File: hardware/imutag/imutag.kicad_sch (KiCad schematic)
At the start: 26 parts, among them J201 CONN_02X04, J301 Conn_01x01, J302 Conn_01x01, J303 Conn_01x01, J304 Conn_01x01, J401 CONN_01X02, Q501 Q_NPN_BEC, U2 AK09940A, U3 LPS22DF, U302 stm32l431kc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

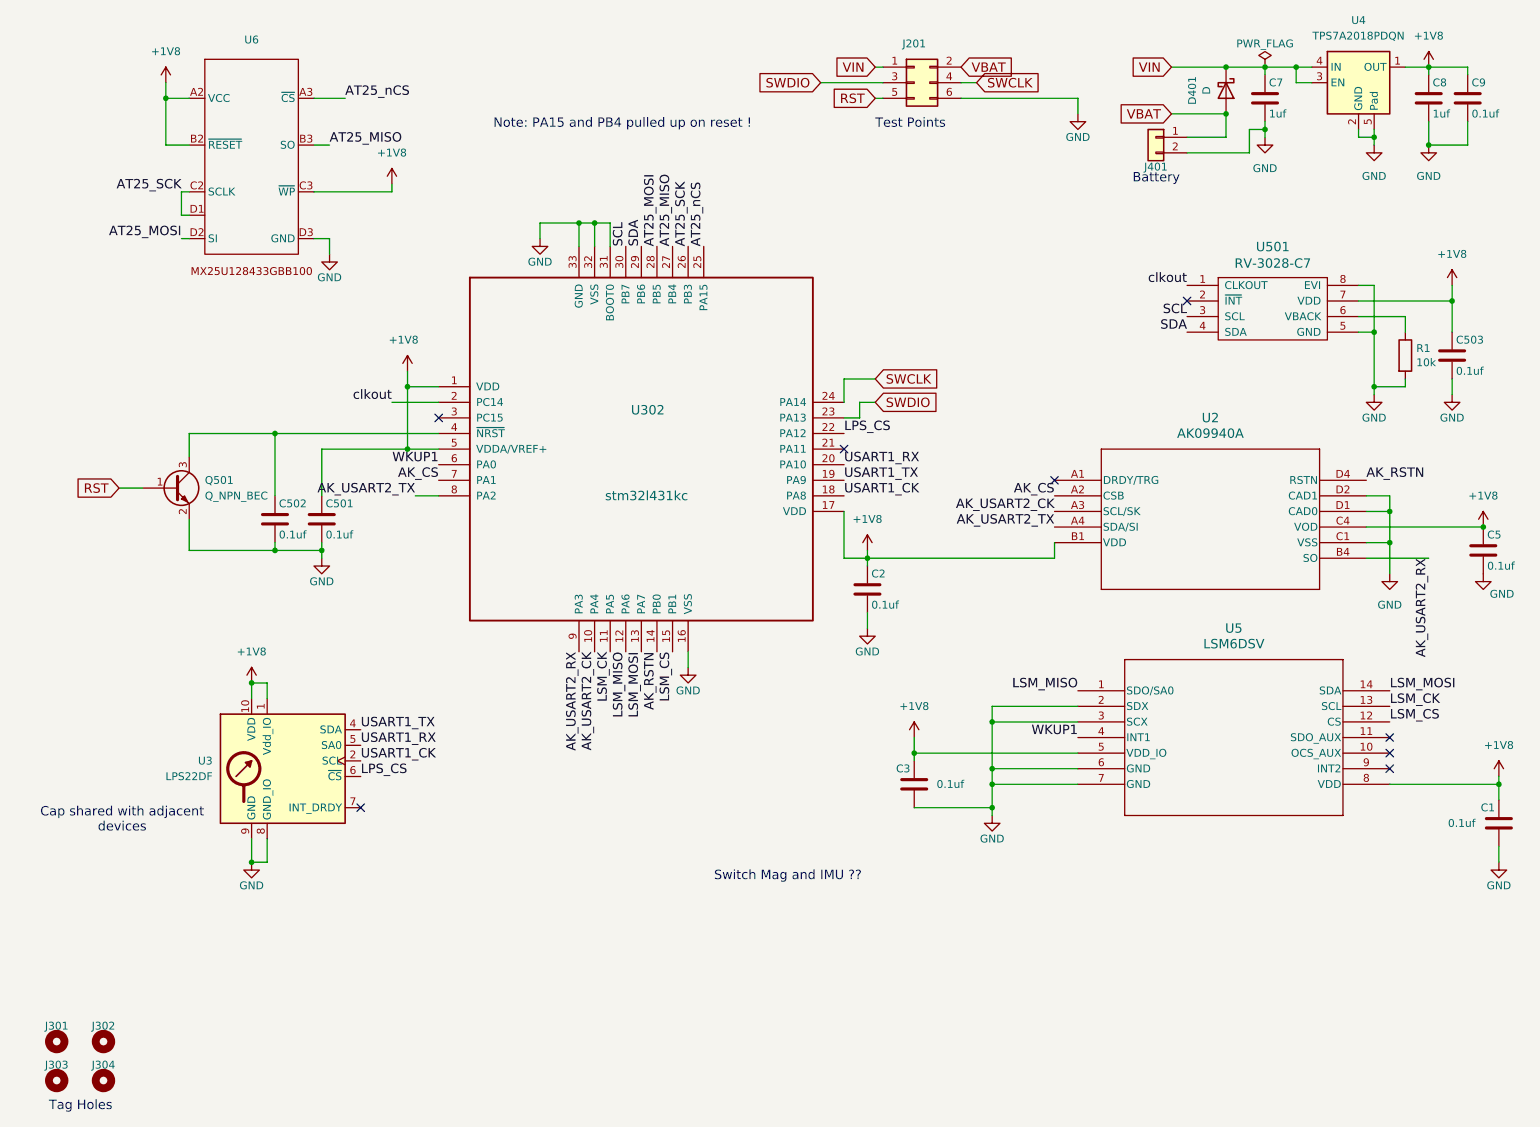
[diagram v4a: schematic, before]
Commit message: imu tag breakout
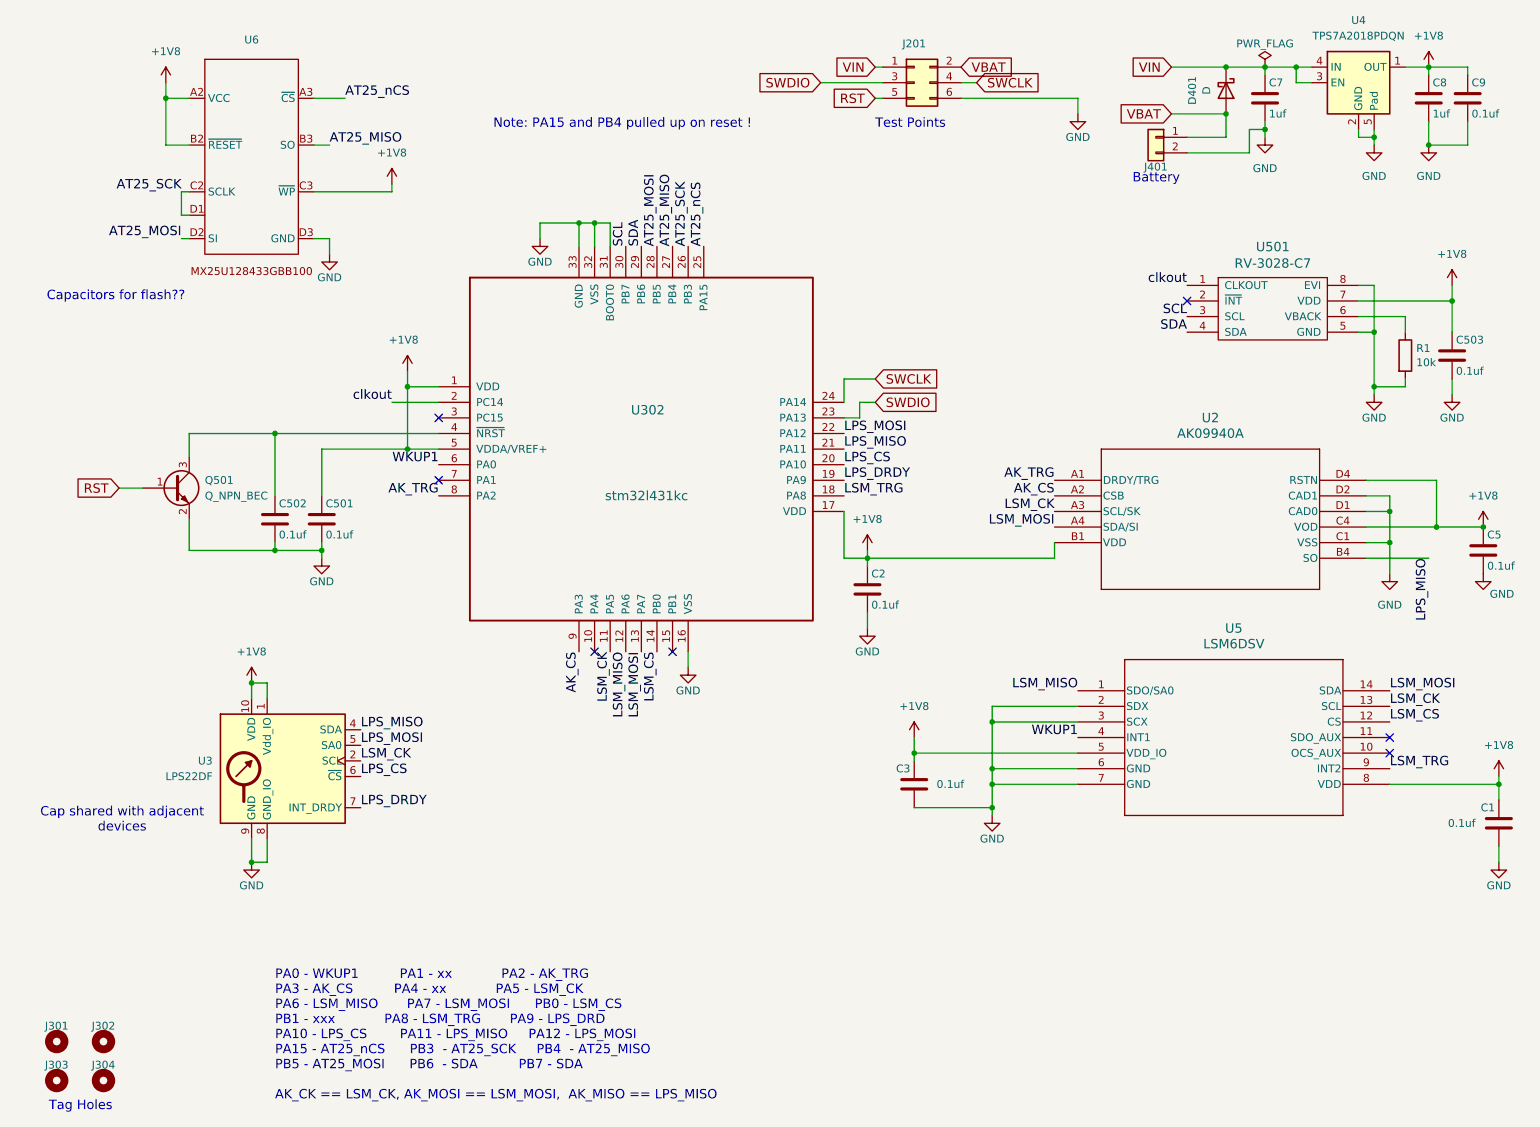
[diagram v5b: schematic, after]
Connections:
- net +1V8: now also U2.D4 (RSTN)
- net AK_CS: now also U302.9 (PA3); no longer U302.7 (PA1)
- net LPS_CS: now also U302.20 (PA10); no longer U302.22 (PA12)
- net LSM_CK: now also U2.A3 (SCL/SK), U3.2 (SCL)
- net LSM_CS: now also U302.14 (PB0); no longer U302.15 (PB1)
- net LSM_MOSI: now also U2.A4 (SDA/SI)
- net LPS_MISO: now reaches U302.21 (PA11)
- net LPS_MISO: now also U2.B4 (SO), U3.4 (SDA)
- net LSM_TRG: now reaches U5.9 (INT2)
- net LSM_TRG: now also U302.18 (PA8)
- net AK_TRG: now reaches U2.A1 (DRDY/TRG)
- net AK_TRG: now also U302.8 (PA2)
- net LPS_DRDY: now reaches U3.7 (INT_DRDY)
- net LPS_DRDY: now also U302.19 (PA9)
- removed net AK_RSTN: U2.D4 (RSTN), U302.14 (PB0)
- net AK_USART2_CK: no longer names the net of U302.10 (PA4)
- net AK_USART2_CK: no longer U2.A3 (SCL/SK)
- removed net AK_USART2_RX: U2.B4 (SO), U302.9 (PA3)
- removed net AK_USART2_TX: U2.A4 (SDA/SI), U302.8 (PA2)
- removed net USART1_CK: U3.2 (SCL), U302.18 (PA8)
- net USART1_RX renamed LPS_MOSI
- net LPS_MOSI: now also U302.22 (PA12); no longer U302.20 (PA10)
- removed net USART1_TX: U3.4 (SDA), U302.19 (PA9)
- no-connect marks 8 -> 7
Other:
- note added: "Capacitors for flash??"
- note added: "PA0 - WKUP1 PA1 - xx PA2 - AK_TRG PA3 - AK_CS PA4 - xx PA5 - LSM_CK PA6 - LSM_MISO PA7 - LSM_MOSI PB0 - LSM_CS PB1 - xxx PA8 - LSM_TRG PA9 - LPS_DRD PA10 - LPS_CS PA11 - LPS_MISO PA12 - LPS_MOSI PA15 - AT25_nCS PB3 - AT25_SCK PB4 - AT25_MISO PB5 - AT25_MOSI PB6 - SDA PB7 - SDA AK_CK == LSM_CK, AK_MOSI == LSM_MOSI, AK_MISO == LPS_MISO"
- note removed: "Switch Mag and IMU ??"
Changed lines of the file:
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@@
 (kicad_sch
-	(version 20231120)
+	(version 20250114)
 	(generator "eeschema")
-	(generator_version "8.0")
+	(generator_version "9.0")
 	(paper "USLetter")
 	(title_block
@@
 		(comment 1 "Geoffrey Brown")
 	)
+	(text "Note: PA15 and PB4 pulled up on reset !"
+		(exclude_from_sim no)
+		(at 96.52 34.29 0)
+		(effects
+			(font
+				(size 1.524 1.524)
+			)
+			(justify left bottom)
+		)
+	)
+	(text "Capacitors for flash??"
+		(exclude_from_sim no)
+		(at 35.052 61.468 0)
+		(effects
+			(font
+				(size 1.524 1.524)
+			)
+		)
+	)
+	(text "Tag Holes"
+		(exclude_from_sim no)
+		(at 24.13 194.31 0)
+		(effects
+			(font
+				(size 1.524 1.524)
+			)
+			(justify left bottom)
+		)
+	)
+	(text "Test Points"
+		(exclude_from_sim no)
+		(at 158.75 34.29 0)
+		(effects
+			(font
+				(size 1.524 1.524)
+			)
+			(justify left bottom)
+		)
+	)
+	(text "PA0 - WKUP1          PA1 - xx            PA2 - AK_TRG\nPA3 - AK_CS          PA4 - xx            PA5 - LSM_CK\nPA6 - LSM_MISO       PA7 - LSM_MOSI      PB0 - LSM_CS\nPB1 - xxx            PA8 - LSM_TRG       PA9 - LPS_DRD\nPA10 - LPS_CS        PA11 - LPS_MISO     PA12 - LPS_MOSI\nPA15 - AT25_nCS      PB3  - AT25_SCK     PB4  - AT25_MISO\nPB5 - AT25_MOSI      PB6  - SDA          PB7 - SDA\n\nAK_CK == LSM_CK, AK_MOSI == LSM_MOSI,  AK_MISO == LPS_MISO"
+		(exclude_from_sim no)
+		(at 60.96 181.864 0)
+		(effects
+			(font
+				(face "Courier")
+				(size 1.524 1.524)
+			)
+			(justify left)
+		)
+	)
+	(text "Battery"
+		(exclude_from_sim no)
+		(at 200.66 43.18 0)
+		(effects
+			(font
+				(size 1.524 1.524)
+			)
+			(justify left bottom)
+		)
+	)
+	(text "Cap shared with adjacent\ndevices"
+		(exclude_from_sim no)
+		(at 36.068 146.812 0)
+		(effects
+			(font
+				(size 1.524 1.524)
+			)
+		)
+	)
 	(junction
 		(at 248.92 24.13)
@@
 	)
 	(junction
+		(at 250.19 99.06)
+		(diameter 0)
+		(color 0 0 0 0)
+	)
+	(junction
 		(at 113.03 49.53)
 		(diameter 0)
@@
 	)
 	(no_connect
-		(at 187.96 91.44)
-	)
-	(no_connect
-		(at 153.67 86.36)
+		(at 113.03 119.38)
 	)
 	(no_connect
-		(at 74.93 144.78)
+		(at 87.63 91.44)
 	)
 	(no_connect
-		(at 242.57 138.43)
+		(at 125.73 119.38)
 	)
 	(no_connect
@@
 	(wire
 		(pts
+			(xy 250.19 99.06) (xy 257.81 99.06)
+		)
+		(stroke
+			(width 0)
+			(type default)
+		)
+	)
+	(wire
+		(pts
 			(xy 207.01 24.13) (xy 215.9 24.13)
 		)
@@
 	(wire
 		(pts
+			(xy 250.19 91.44) (xy 250.19 99.06)
+		)
+		(stroke
+			(width 0)
+			(type default)
+		)
+	)
+	(wire
+		(pts
 			(xy 82.55 73.66) (xy 82.55 76.2)
 		)
@@
 	(wire
 		(pts
+			(xy 238.76 91.44) (xy 250.19 91.44)
+		)
+		(stroke
+			(width 0)
+			(type default)
+		)
+	)
+	(wire
+		(pts
 			(xy 237.49 64.77) (xy 245.11 64.77)
 		)
@@
 	(wire
 		(pts
-			(xy 238.76 99.06) (xy 257.81 99.06)
+			(xy 238.76 99.06) (xy 250.19 99.06)
 		)
 		(stroke
@@
 	(wire
 		(pts
-			(xy 83.82 93.98) (xy 87.63 93.98)
-		)
-		(stroke
-			(width 0)
-			(type default)
-		)
-	)
-	(wire
-		(pts
 			(xy 69.85 52.07) (xy 69.85 54.61)
 		)
@@
 		)
 	)
-	(text "Note: PA15 and PB4 pulled up on reset !"
-		(exclude_from_sim no)
-		(at 96.52 34.29 0)
-		(effects
-			(font
-				(size 1.524 1.524)
-			)
-			(justify left bottom)
-		)
-	)
-	(text "Tag Holes"
-		(exclude_from_sim no)
-		(at 24.13 194.31 0)
-		(effects
-			(font
-				(size 1.524 1.524)
-			)
-			(justify left bottom)
-		)
-	)
-	(text "Test Points"
-		(exclude_from_sim no)
-		(at 158.75 34.29 0)
-		(effects
-			(font
-				(size 1.524 1.524)
-			)
-			(justify left bottom)
-		)
-	)
-	(text "Battery"
-		(exclude_from_sim no)
-		(at 200.66 43.18 0)
-		(effects
-			(font
-				(size 1.524 1.524)
-			)
-			(justify left bottom)
-		)
-	)
-	(text "Switch Mag and IMU ??"
-		(exclude_from_sim no)
-		(at 144.526 155.956 0)
-		(effects
-			(font
-				(size 1.524 1.524)
-			)
-		)
-	)
-	(text "Cap shared with adjacent\ndevices"
-		(exclude_from_sim no)
-		(at 36.068 146.812 0)
-		(effects
-			(font
-				(size 1.524 1.524)
-			)
-		)
-	)
-	(label "USART1_CK"
-		(at 153.67 93.98 0)
-		(effects
-			(font
-				(size 1.524 1.524)
-			)
-			(justify left bottom)
-		)
-	)
-	(label "USART1_TX"
-		(at 153.67 91.44 0)
-		(effects
-			(font
-				(size 1.524 1.524)
-			)
-			(justify left bottom)
-		)
-	)
 	(label "LSM_CK"
 		(at 115.57 119.38 270)
@@
 		)
 	)
-	(label "AK_RSTN"
-		(at 123.19 119.38 270)
-		(effects
-			(font
-				(size 1.524 1.524)
-			)
-			(justify right bottom)
-		)
-	)
-	(label "USART1_CK"
+	(label "LSM_CK"
 		(at 74.93 137.16 0)
 		(effects
@@
 		)
 	)
-	(label "USART1_RX"
-		(at 153.67 88.9 0)
+	(label "LPS_DRDY"
+		(at 153.67 91.44 0)
 		(effects
 			(font
@@
 		)
 	)
-	(label "AK_USART2_RX"
-		(at 110.49 119.38 270)
+	(label "LSM_MISO"
+		(at 191.77 125.73 180)
 		(effects
 			(font
@@
 		)
 	)
-	(label "LSM_MISO"
-		(at 191.77 125.73 180)
+	(label "AK_CS"
+		(at 187.96 93.98 180)
 		(effects
 			(font
@@
 		)
 	)
-	(label "AK_CS"
-		(at 187.96 93.98 180)
+	(label "clkout"
+		(at 80.01 78.74 180)
 		(effects
 			(font
@@
 		)
 	)
-	(label "clkout"
-		(at 80.01 78.74 180)
+	(label "AK_TRG"
+		(at 187.96 91.44 180)
+		(effects
+			(font
+				(size 1.524 1.524)
+			)
+			(justify right bottom)
+		)
+	)
+	(label "AK_CS"
+		(at 110.49 119.38 270)
 		(effects
 			(font
@@
 	)
 	(label "LSM_CS"
-		(at 125.73 119.38 270)
+		(at 123.19 119.38 270)
 		(effects
 			(font
@@
 		)
 	)
-	(label "AK_USART2_CK"
-		(at 113.03 119.38 270)
+	(label "LPS_DRDY"
+		(at 74.93 144.78 0)
 		(effects
 			(font
 				(size 1.524 1.524)
 			)
-			(justify right bottom)
+			(justify left bottom)
 		)
 	)
-	(label "AK_CS"
-		(at 87.63 91.44 180)
+	(label "LSM_TRG"
+		(at 153.67 93.98 0)
+		(effects
+			(font
+				(size 1.524 1.524)
+			)
+			(justify left bottom)
+		)
+	)
+	(label "AK_TRG"
+		(at 87.63 93.98 180)
 		(effects
 			(font
@@
 		)
 	)
-	(label "AK_USART2_CK"
+	(label "LSM_CK"
 		(at 187.96 96.52 180)
 		(effects
@@
 		)
 	)
-	(label "USART1_TX"
+	(label "LPS_MISO"
 		(at 74.93 132.08 0)
 		(effects
@@
 	)
 	(label "LPS_CS"
-		(at 153.67 83.82 0)
+		(at 153.67 88.9 0)
 		(effects
 			(font
@@
 		)
 	)
-	(label "AT25_SCK"
-		(at 128.27 53.34 90)
+	(label "LPS_MISO"
+		(at 153.67 86.36 0)
 		(effects
 			(font
@@
 		)
 	)
-	(label "AT25_MISO"
-		(at 69.85 36.83 0)
+	(label "LPS_MOSI"
+		(at 153.67 83.82 0)
 		(effects
 			(font
@@
 		)
 	)
-	(label "AK_RSTN"
-		(at 238.76 91.44 0)
+	(label "LSM_TRG"
+		(at 242.57 138.43 0)
 		(effects
 			(font
@@
 		)
 	)
-	(label "AK_USART2_TX"
-		(at 187.96 99.06 180)
+	(label "AT25_SCK"
+		(at 128.27 53.34 90)
 		(effects
 			(font
 				(size 1.524 1.524)
 			)
-			(justify right bottom)
+			(justify left bottom)
 		)
 	)
-	(label "SCL"
-		(at 209.55 64.77 180)
+	(label "AT25_MISO"
+		(at 69.85 36.83 0)
+		(effects
+			(font
+				(size 1.524 1.524)
+			)
+			(justify left bottom)
+		)
+	)
+	(label "LSM_MOSI"
+		(at 187.96 99.06 180)
 		(effects
 			(font
@@
 		)
 	)
-	(label "LSM_MISO"
-		(at 118.11 119.38 270)
+	(label "SCL"
+		(at 209.55 64.77 180)
 		(effects
 			(font
@@
 		)
 	)
-	(label "AK_USART2_TX"
-		(at 83.82 93.98 180)
+	(label "LSM_MISO"
+		(at 118.11 119.38 270)
 		(effects
 			(font
@@
 		)
 	)
-	(label "AK_USART2_RX"
+	(label "LPS_MISO"
 		(at 248.92 104.14 270)
 		(effects
@@
 		)
 	)
-	(label "USART1_RX"
+	(label "LPS_MOSI"
 		(at 74.93 134.62 0)
 		(effects
@@
 		)
 	)
+	(embedded_fonts no)
 )

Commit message: checkpoint
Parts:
- added C4: 4.7uf, Capacitor_SMD:C_0201_0603Metric, symbol Device:C
- C1, C3, C501, C502, C503: MPN C181047 -> GRM033C81E104KE14D
- C2: LCSC C76929 -> C181047; MFN murata -> Murata; MPN GRM033R60J105MEA2D -> GRM033C81E104KE14D
- C5, C9: LCSC (none) -> C181047
- C7, C8: LCSC (none) -> C76930
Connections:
- net GND: now also C4.1; no longer U302.31 (BOOT0)
- new net: C4.2, U302.31 (BOOT0)
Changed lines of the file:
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@@
 	)
 	(junction
+		(at 104.14 49.53)
+		(diameter 0)
+		(color 0 0 0 0)
+	)
+	(junction
 		(at 177.8 130.81)
 		(diameter 0)
@@
 	)
 	(junction
-		(at 113.03 49.53)
-		(diameter 0)
-		(color 0 0 0 0)
-	)
-	(junction
 		(at 260.35 140.97)
 		(diameter 0)
@@
 	(wire
 		(pts
+			(xy 104.14 41.91) (xy 115.57 41.91)
+		)
+		(stroke
+			(width 0)
+			(type default)
+		)
+	)
+	(wire
+		(pts
 			(xy 260.35 140.97) (xy 260.35 143.51)
 		)
@@
 	(wire
 		(pts
-			(xy 113.03 49.53) (xy 115.57 49.53)
-		)
-		(stroke
-			(width 0)
-			(type default)
-		)
-	)
-	(wire
-		(pts
 			(xy 238.76 93.98) (xy 242.57 93.98)
 		)
@@
 	(wire
 		(pts
-			(xy 115.57 49.53) (xy 115.57 53.34)
+			(xy 115.57 41.91) (xy 115.57 53.34)
 		)
 		(stroke
@@
 			)
 		)
-		(property "MPN" "C181047"
+		(property "MPN" "GRM033C81E104KE14D"
 			(at 60.96 97.79 0)
 			(effects
@@
 			)
 		)
-		(property "MPN" "C181047"
+		(property "MPN" "GRM033C81E104KE14D"
 			(at 68.58 97.79 0)
 			(effects
@@
 			)
 		)
-		(property "MPN" "C181047"
+		(property "MPN" "GRM033C81E104KE14D"
 			(at 252.73 71.12 0)
 			(effects
@@
 			)
 		)
-		(property "MPN" "C181047"
+		(property "MPN" "GRM033C81E104KE14D"
 			(at 438.15 250.19 0)
 			(effects
@@
 			)
 		)
-		(property "MFN" "murata"
+		(property "MFN" "Murata"
 			(at 157.48 109.22 0)
 			(effects
@@
 			)
 		)
-		(property "MPN" "GRM033R60J105MEA2D"
+		(property "MPN" "GRM033C81E104KE14D"
 			(at 157.48 109.22 0)
 			(effects
@@
 			)
 		)
-		(property "LCSC" "C76929"
+		(property "LCSC" "C181047"
 			(at 157.48 109.22 0)
 			(effects
@@
 			)
 		)
+		(property "LCSC" "C181047"
+			(at 255.27 29.21 0)
+			(effects
+				(font
+					(size 1.27 1.27)
+				)
+				(hide yes)
+			)
+		)
 		(pin "1"
 		)
@@
 			)
 		)
+		(property "LCSC" "C76930"
+			(at 248.92 29.21 0)
+			(effects
+				(font
+					(size 1.27 1.27)
+				)
+				(hide yes)
+			)
+		)
 		(pin "1"
 		)
@@
 			)
 		)
+		(property "LCSC" "C181047"
+			(at 257.81 102.87 0)
+			(effects
+				(font
+					(size 1.27 1.27)
+				)
+				(hide yes)
+			)
+		)
 		(pin "1"
 		)
@@
 			)
 		)
+		(property "LCSC" "C76930"
+			(at 222.25 29.21 0)
+			(effects
+				(font
+					(size 1.27 1.27)
+				)
+				(hide yes)
+			)
+		)
 		(pin "1"
 		)
@@
 	)
 	(symbol
+		(lib_id "Device:C")
+		(at 104.14 45.72 180)
+		(unit 1)
+		(exclude_from_sim no)
+		(in_bom yes)
+		(on_board yes)
+		(dnp no)
+		(fields_autoplaced yes)
+		(property "Reference" "C4"
+			(at 107.95 44.4499 0)
+			(effects
+				(font
+					(size 1.27 1.27)
+				)
+				(justify right)
+			)
+		)
+		(property "Value" "4.7uf"
+			(at 107.95 46.9899 0)
+			(effects
+				(font
+					(size 1.27 1.27)
+				)
+				(justify right)
+			)
+		)
+		(property "Footprint" "Capacitor_SMD:C_0201_0603Metric"
+			(at 103.1748 41.91 0)
+			(effects
+				(font
+					(size 1.27 1.27)
+				)
+				(hide yes)
+			)
+		)
+		(property "Datasheet" "~"
+			(at 104.14 45.72 0)
+			(effects
+				(font
+					(size 1.27 1.27)
+				)
+				(hide yes)
+			)
+		)
+		(property "Description" "Unpolarized capacitor"
+			(at 104.14 45.72 0)
+			(effects
+				(font
+					(size 1.27 1.27)
+				)
+				(hide yes)
+			)
+		)
+		(property "LCSC" "C335103"
+			(at 104.14 45.72 0)
+			(effects
+				(font
+					(size 1.27 1.27)
+				)
+				(hide yes)
+			)
+		)
+		(property "MFN" "Murata"
+			(at 104.14 45.72 0)
+			(effects
+				(font
+					(size 1.27 1.27)
+				)
+				(hide yes)
+			)
+		)
+		(property "MPN" "GRM035R60J475ME15D"
+			(at 104.14 45.72 0)
+			(effects
+				(font
+					(size 1.27 1.27)
+				)
+				(hide yes)
+			)
+		)
+		(pin "1"
+		)
+		(pin "2"
+		)
+		(instances
+			(project ""
+				(path "/e44ca67a-43be-444b-8652-f54825a2eb6f"
+					(reference "C4")
+					(unit 1)
+				)
+			)
+		)
+	)
+	(symbol
 		(lib_id "power:GND")
 		(at 240.03 77.47 0)
@@
 			)
 		)
-		(property "MPN" "C181047"
+		(property "MPN" "GRM033C81E104KE14D"
 			(at 342.9 243.84 0)
 			(effects

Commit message: checkpoint
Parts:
- U4: value TPS7A2018PDQN -> TPS7A0218PDQNR; DISTPN 296-TPS7A2018PDQNRCT-ND -> 296-TPS7A0218PDQNRTR-ND; LCSC (none) -> C2862166; MPN TPS7A2018PDQNR -> TPS7A0218PDQNR
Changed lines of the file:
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@@
 			)
 		)
-		(property "Value" "TPS7A2018PDQN"
+		(property "Value" "TPS7A0218PDQNR"
 			(at 237.49 19.05 0)
 			(effects
@@
 			)
 		)
-		(property "Datasheet" "https://www.ti.com/lit/ds/symlink/tps7a20.pdf"
+		(property "Datasheet" "https://www.ti.com/cn/lit/ds/symlink/tps7a02.pdf?ts=1774837401876&ref_url=https%253A%252F%252Fso.szlcsc.com%252F"
 			(at 237.49 13.97 0)
 			(effects
@@
 			)
 		)
-		(property "MPN" "TPS7A2018PDQNR"
+		(property "MPN" "TPS7A0218PDQNR"
 			(at 237.49 26.67 0)
 			(effects
@@
 			)
 		)
-		(property "DISTPN" "296-TPS7A2018PDQNRCT-ND"
+		(property "DISTPN" "296-TPS7A0218PDQNRTR-ND"
 			(at 237.49 26.67 0)
 			(effects
@@
 				)
 				(hide yes)
+			)
+		)
+		(property "LCSC" " C2862166"
+			(at 237.49 26.67 0)
+			(effects
+				(font
+					(size 1.524 1.524)
+				)
+				(hide yes)
